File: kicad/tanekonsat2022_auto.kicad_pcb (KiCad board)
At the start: 2 copper layers, 88 parts, among them IC1 W25Q128JVSIQ, IC2 ADP3338AKCZ-3.3-RL, IC3 NJM12888F18, IC4 TESEO-LIV3F, IC5 CGGBPD.25.A, IC6 MAX2641EUT+T, IC7 TB67H450FNG,EL, IC8 TB67H450FNG,EL, J1 Conn_01x02_Male, J2 USB_B_Micro, J3 Conn_01x02_Male, J4 Conn_01x02_Male, J5 Conn_01x06_Female, J6 Conn_01x06_Female, J7 Conn_01x04_Female, Q1 Q_NMOS_DGS, Q2 Q_NMOS_DGS, Q3 BSS138, Q4 BSS138, Q5 BSS138, Q6 BSS138, Q7 Q_NMOS_DGS, SW1 SW_DIP_x01, U1 RP2040, U2 CR1025, U3 VL53L5X_SL, U4 ICM-20948_SL, Y1 FA-238V_12.0000MB-K3

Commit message: done! AW of GNSS board
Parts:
- removed C26: 56p, Capacitor_SMD:C_0201_0603Metric
- added J8: Conn_01x02_Female, Connector_PinHeader_2.00mm:PinHeader_1x02_P2.00mm_Vertical, F.Cu at (177.6, 49.7)
- C19, C20, C21, D1, D2, IC2, IC7, IC8, R18, R19, R20, R21: moved to B.Cu
- C2, C5: value 27p -> 10p
- J1: footprint Connector_JST:JST_PH_B3B-PH-K_1x03_P2.00mm_Vertical -> Connector_JST:JST_PH_S3B-PH-K_1x03_P2.00mm_Horizontal; moved to B.Cu
- J3, J4: footprint Connector_PinHeader_2.00mm:PinHeader_1x02_P2.00mm_Vertical -> tanekonsat:PinHeader_1x02_P2.00mm_Vertical
- J5, J6: footprint Connector_PinHeader_2.00mm:PinHeader_1x06_P2.00mm_Vertical -> tanekonsat:PinHeader_1x06_P2.00mm_Vertical; moved to B.Cu
- moved J5 93.3 mm to (129.2, 91.4), turned to -90 degrees
- moved U3 89.5 mm to (138.4, 60.0)
- moved J6 82.2 mm to (116.2, 91.4), turned to -90 degrees
- moved C21 79.0 mm to (116.1, 86.4)
- moved C20 75.5 mm to (107.9, 75.2), turned to 180 degrees
- moved C29 71.8 mm to (169.0, 51.1)
- moved Q2 69.8 mm to (80.5, 86.9)
- moved L2 69.8 mm to (173.7, 54.5)
- moved C27 69.1 mm to (171.1, 49.1), turned to 90 degrees
- moved R19 67.6 mm to (125.6, 89.2), turned to 180 degrees
- moved C18 66.3 mm to (115.6, 88.9), turned to 90 degrees
- moved IC1 66.0 mm to (134.4, 74.7), turned to -90 degrees
- moved C19 64.3 mm to (107.9, 77.7), turned to 180 degrees
- moved R20 63.5 mm to (126.5, 85.9)
- moved IC7 62.9 mm to (131.1, 86.1), turned to -90 degrees
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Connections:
- C29 pad 1: +3V3 -> /VCC_RF
- C29 pad 2: +3V3 -> GND2
- IC4 pad 14: Net-(C26-Pad1) -> /VCC_RF
- IC4 pad 16: unconnected-(IC4-Pad16) -> Net-(IC4-Pad16)
- IC4 pad 17: unconnected-(IC4-Pad17) -> Net-(IC4-Pad17)
- IC6 pad 6: +3V3 -> /VCC_RF
- IC7 pad 3: /GPIO13_MO_A_2 -> /GPIO12_MO_A_1
- IC7 pad 6: Net-(IC7-Pad6) -> /M1_MINUS
- IC7 pad 8: Net-(IC7-Pad8) -> /M1_PLUS
- IC8 pad 2: /GPIO14_MO_B_1 -> /GPIO15_MO_B_2
- IC8 pad 3: /GPIO15_MO_B_2 -> /GPIO14_MO_B_1
- IC8 pad 6: Net-(IC8-Pad6) -> /M2_MINUS
- IC8 pad 8: Net-(IC8-Pad8) -> /M2_PLUS
- J5 pad 1: /GPIO13_MO_A_2 -> /M1_PLUS
- J5 pad 2: /GPIO13_MO_A_2 -> /M1_MINUS
- J5 pad 4: /GPIO21_MOE_A_1 -> /GPIO20_MOE_A_1
- J5 pad 5: /GPIO20_MOE_A_2 -> /GPIO21_MOE_A_2
- J6 pad 1: /GPIO14_MO_B_1 -> /M2_PLUS
- J6 pad 2: /GPIO15_MO_B_2 -> /M2_MINUS
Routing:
- net +3V0: track 0.00 -> 30.9 mm
- net GND2: track 0.00 -> 23.4 mm, vias 0 -> 101
- net /VCC_RF: track 0.00 -> 13.5 mm
- net +3V3: track 0.00 -> 5.58 mm
- net Net-(C28-Pad2): track 0.00 -> 3.73 mm
- net /GPIO4_GNSS_TX: track 0.00 -> 3.36 mm
- net Net-(C24-Pad1): track 0.00 -> 3.35 mm
- net Net-(IC4-Pad16): track 0.00 -> 3.05 mm
- net /GPIO5_GNSS_RX: track 0.00 -> 2.99 mm
- net Net-(IC4-Pad17): track 0.00 -> 2.67 mm
- net Net-(C28-Pad1): track 0.00 -> 1.96 mm
- net Net-(IC6-Pad1): track 0.00 -> 1.68 mm
- net Net-(C27-Pad2): track 0.00 -> 1.60 mm
- net Net-(C27-Pad1): track 0.00 -> 1.40 mm
- net Net-(C25-Pad2): track 0.00 -> 1.27 mm
- added copper zone on B.Cu, net GND2
- added copper zone on F.Cu, net GND2
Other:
- board outline added: 76.6 x 67.8 mm
- board text added: "+3V3"
- board text added: "DERC"
- board text added: "Design: Akio M"
- board text added: "GND"
- board text added: "GNSS Board"
- board text added: "I2C"
- board text added: "RX"
- board text added: "SCL"
- board text added: "SDA"
- board text added: "TX"
- board text added: "UART"
- board text added: "tanekonsat2022"

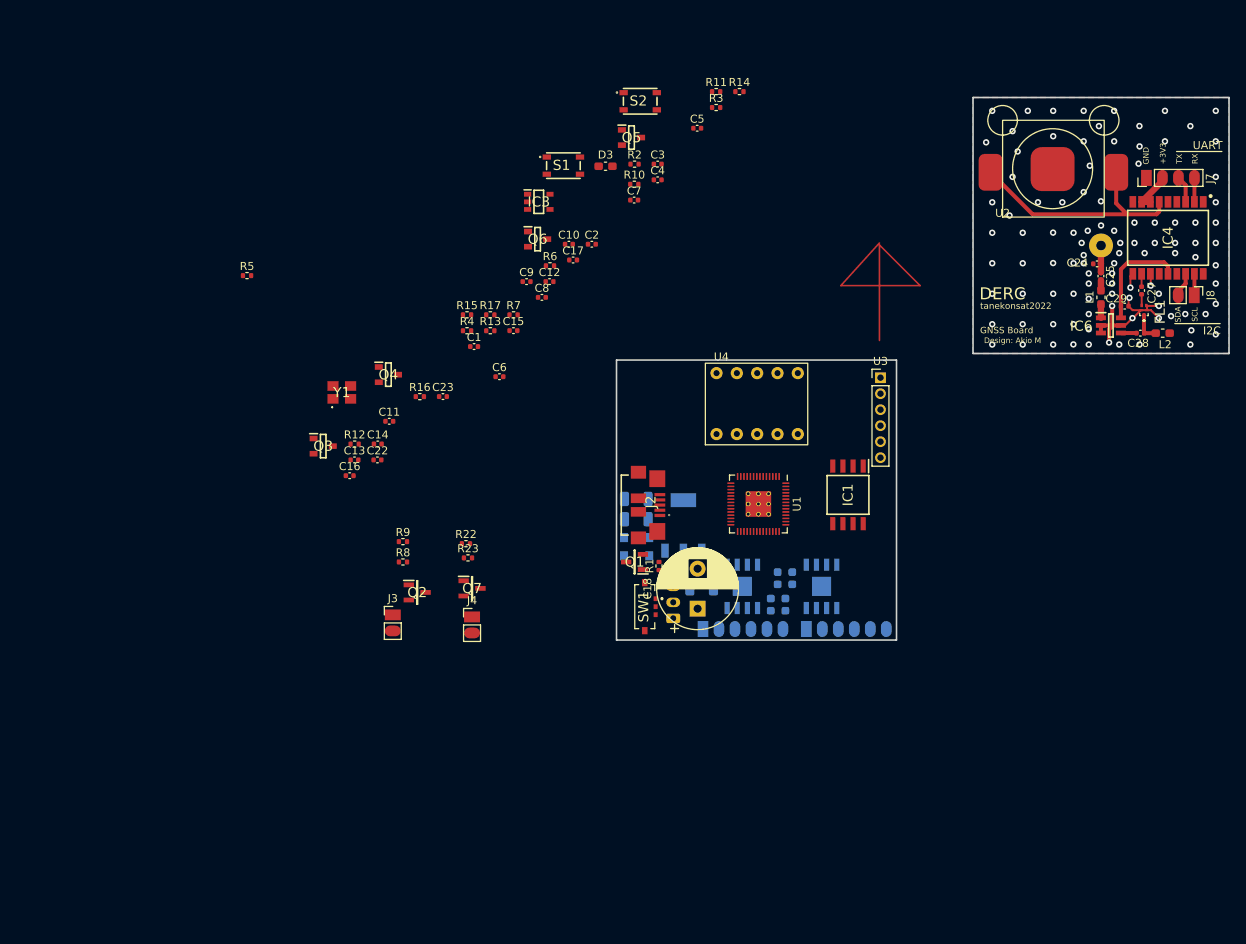
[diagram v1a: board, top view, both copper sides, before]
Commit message: update 9-axis sensor
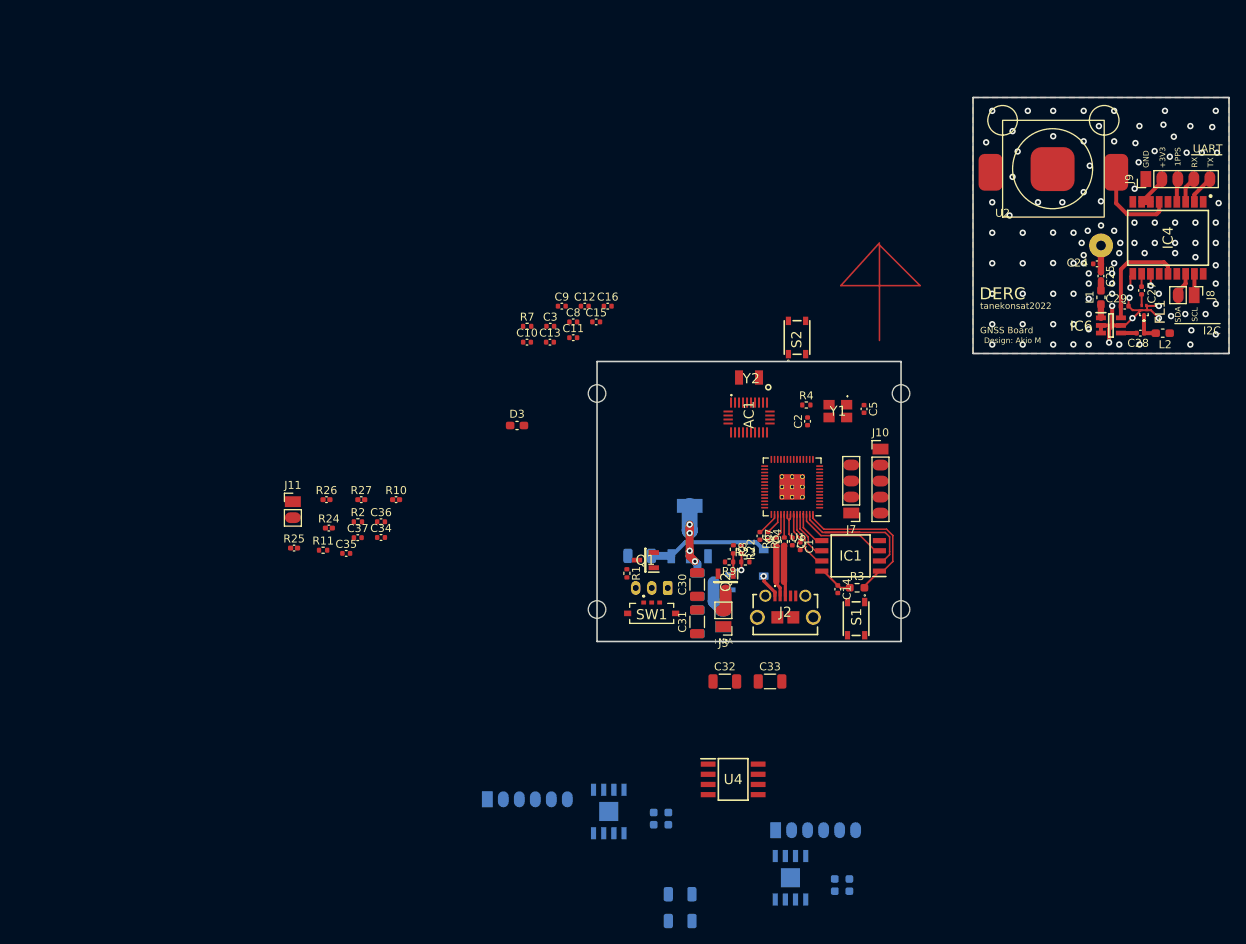
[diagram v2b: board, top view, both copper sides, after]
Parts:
- removed C17, C23: 1u, Capacitor_SMD:C_0402_1005Metric
- removed C22: 0.01u, Capacitor_SMD:C_0402_1005Metric
- removed D2: SS2040FL_R1_00001, SamacSys_Parts:SODFL3618X110N
- removed IC3: NJM12888F18, SamacSys_Parts:SOT95P280X130-5N
- removed Q3, Q4, Q5, Q6: BSS138, SamacSys_Parts:SOT95P240X120-3N
- removed R12, R13, R14, R15, R16, R17: 10k, Resistor_SMD:R_0402_1005Metric
- removed U3: VL53L5X_SL, Connector_PinHeader_2.00mm:PinHeader_1x06_P2.00mm_Vertical
- added AC1: BNO085, tanekonsat:BNO085, F.Cu at (122.0, 65.0)
- added C26: 100u, Capacitor_SMD:C_1206_3216Metric, B.Cu at (113.4, 127.9)
- added C30: 100u, Capacitor_SMD:C_1206_3216Metric, F.Cu at (115.5, 85.9)
- added C31: 100u, Capacitor_SMD:C_1206_3216Metric, F.Cu at (115.5, 90.6)
- added C32: 100u, Capacitor_SMD:C_1206_3216Metric, F.Cu at (119.0, 98.0)
- added C33: 100u, Capacitor_SMD:C_1206_3216Metric, F.Cu at (124.6, 98.0)
- added C34: 100n, Capacitor_SMD:C_0402_1005Metric, F.Cu at (76.0, 80.0)
- added C35: 22p, Capacitor_SMD:C_0402_1005Metric, F.Cu at (71.7, 82.0)
- added C36: 22p, Capacitor_SMD:C_0402_1005Metric, F.Cu at (76.0, 78.0)
- added C37: 100n, Capacitor_SMD:C_0402_1005Metric, F.Cu at (73.1, 80.0)
- added J10: Conn_01x05_Female, tanekonsat:PinHeader_1x05_P2.00mm_Vertical, F.Cu at (138.4, 68.9)
- added J11: Conn_01x02_Female, tanekonsat:PinHeader_1x02_P2.00mm_Vertical, F.Cu at (65.0, 75.5)
- added J9: Conn_01x05_Female, tanekonsat:PinHeader_1x05_P2.00mm_Vertical, F.Cu at (171.6, 35.2)
- added R24: 0, tanekonsat:Jumper_0402_1005Metric, F.Cu at (69.5, 78.8)
- added R25: 0, tanekonsat:Jumper_0402_1005Metric, F.Cu at (65.1, 81.3)
- added R26: 0, tanekonsat:Jumper_0402_1005Metric, F.Cu at (69.2, 75.3)
- added R27: 0, tanekonsat:Jumper_0402_1005Metric, F.Cu at (73.5, 75.3)
- added REF**: MountingHole_2.2mm_M2, MountingHole:MountingHole_2.2mm_M2, F.Cu at (141.0, 89.0)
- added REF**: MountingHole_2.2mm_M2, MountingHole:MountingHole_2.2mm_M2, F.Cu at (103.0, 89.0)
- added REF**: MountingHole_2.2mm_M2, MountingHole:MountingHole_2.2mm_M2, F.Cu at (141.0, 62.0)
- added REF**: MountingHole_2.2mm_M2, MountingHole:MountingHole_2.2mm_M2, F.Cu at (103.0, 62.0)
- added Y2: FC-135_32.768KHz_7pF_+_-20ppm, SamacSys_Parts:FC-135, F.Cu at (122.0, 60.0)
- C18: value 1000u -> 100u; footprint Capacitor_THT:CP_Radial_D10.0mm_P5.00mm -> Capacitor_SMD:C_1206_3216Metric; moved to B.Cu
- D1: value SS2040FL_R1_00001 -> 1N4148W; footprint SamacSys_Parts:SODFL3618X110N -> Diode_SMD:D_SOD-123
- J2: footprint SamacSys_Parts:ZX62R-B-5P_30_ -> SamacSys_Parts:101181940001LFBKN
- J4, Q7: moved to B.Cu
- J7: footprint Connector_PinHeader_2.00mm:PinHeader_1x04_P2.00mm_Vertical -> tanekonsat:PinHeader_1x04_P2.00mm_Vertical
- R10: value 10k -> 0; footprint Resistor_SMD:R_0402_1005Metric -> tanekonsat:Jumper_0402_1005Metric
- R3: value 10k -> DNF; footprint Resistor_SMD:R_0402_1005Metric -> Resistor_SMD:R_0603_1608Metric_Pad0.98x0.95mm_HandSolder
- U4: value ICM-20948_SL -> ACPL-224-500E; footprint tanekonsat:ICM-20948_SL -> SamacSys_Parts:SOIC127P700X220-8N
- moved R11 75.5 mm to (68.8, 81.6)
- moved R5 74.9 mm to (126.4, 80.5), turned to 90 degrees
- moved S1 67.4 mm to (135.4, 90.1), turned to -90 degrees
- moved R3 62.6 mm to (135.5, 86.3)
- moved Y1 62.0 mm to (133.1, 64.2), turned to 180 degrees
- moved C14 60.3 mm to (133.1, 86.5), turned to -90 degrees
- moved R2 56.5 mm to (73.1, 78.0)
- moved J7 55.8 mm to (134.8, 76.9), turned to 180 degrees
- moved R10 49.4 mm to (77.9, 75.3)
- moved C1 47.8 mm to (128.4, 81.1), turned to -90 degrees
- moved C4 46.6 mm to (124.4, 79.8), turned to -90 degrees
- moved C7 44.8 mm to (123.4, 79.8), turned to -90 degrees
- moved R6 44.6 mm to (125.4, 80.5), turned to 90 degrees
- moved R4 43.4 mm to (129.2, 63.4)
- moved C6 42.0 mm to (127.4, 80.5), turned to -90 degrees
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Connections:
- net /GPIO24_Nichrome renamed /GPIO24_NichromeB
- net /GPIO4_GNSS_TX renamed /GPIO4_GNSS_RX
- net /GPIO5_GNSS_RX renamed /GPIO5_GNSS_TX
- C18 pad 1: /+7V4 -> /V_REG
- C2 pad 1: Net-(C2-Pad1) -> GND
- C2 pad 2: GND -> /XIN
- C21 pad 1: +3V3 -> /V_REG
- D1 pad 2: /+7V4 -> /VBUS
- IC4 pad 4: unconnected-(IC4-Pad4) -> /GNSS_1PPS
- IC7 pad 2: /GPIO13_MO_A_2 -> Net-(IC7-Pad2)
- IC7 pad 3: /GPIO12_MO_A_1 -> Net-(IC7-Pad3)
- IC7 pad 5: /+7V4 -> /V_REG
- IC8 pad 2: /GPIO15_MO_B_2 -> Net-(IC8-Pad2)
- IC8 pad 3: /GPIO14_MO_B_1 -> Net-(IC8-Pad3)
- IC8 pad 5: /+7V4 -> /V_REG
- J1 pad 1: /+7V4 -> /V_REG
- J3 pad 1: /+7V4 -> /V_REG
- J4 pad 1: /+7V4 -> /V_REG
- R10 pad 1: +3V3 -> GND
- R10 pad 2: /GPIO18_M_SCK -> GND3
- R11 pad 2: /GPIO19_M_SDI_RX -> Net-(AC1-Pad4)
- R4 pad 2: Net-(R4-Pad2) -> Net-(C5-Pad1)
- R7 pad 1: /GPIO25_LED -> /GPIO3_LED
- R8 pad 1: /GPIO3_Nichrome -> /GPIO25_NichromeA
- SW1 pad 2: /+7V4 -> /V_REG
- U1 pad 13: /GPIO10 -> /GPIO10_I2C_EXT_SDA
- U1 pad 14: /GPIO11 -> /GPIO11_I2C_EXT_SCL
- U1 pad 27: /GPIO16_M_SDO_TX -> /GPIO16_IMU_MISO
- U1 pad 28: /GPIO17_M_CS -> /GPIO17_IMU_CS
- U1 pad 29: /GPIO18_M_SCK -> /GPIO18_IMU_SCK
- U1 pad 30: /GPIO19_M_SDI_RX -> /GPIO19_IMU_MOSI
- U1 pad 37: /GPIO25_LED -> /GPIO25_NichromeA
- U1 pad 5: /GPIO3_Nichrome -> /GPIO3_LED
- U1 pad 8: /GPIO6 -> /GPIO6_IMU_INT
- U1 pad 9: /GPIO7 -> /GPIO7_IMU_RST
- U4 pad 1: +1V8 -> /GPIO13_MO_A_2
- U4 pad 2: +1V8 -> /GPIO12_MO_A_1
- U4 pad 3: /IMU_SCLK -> /GPIO15_MO_B_2
- U4 pad 4: /IMU_SDI -> /GPIO14_MO_B_1
- U4 pad 5: /IMU_SDO -> Net-(IC8-Pad3)
- U4 pad 6: /IMU_CS -> Net-(IC8-Pad2)
- U4 pad 7: unconnected-(U4-Pad7) -> Net-(IC7-Pad3)
- U4 pad 8: unconnected-(U4-Pad8) -> Net-(IC7-Pad2)
- Y1 pad 1: Net-(R4-Pad2) -> Net-(C5-Pad1)
- Y1 pad 2: Net-(C2-Pad1) -> GND
- Y1 pad 4: Net-(C5-Pad1) -> GND
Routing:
- net +3V3: track 5.58 -> 28.9 mm, vias 0 -> 4
- net /QSPI_SD1: track 0.00 -> 19.8 mm
- net /QSPI_SS: track 0.00 -> 19.6 mm
- net +3V0: track 30.9 -> 11.7 mm
- net /V_REG: track 0.00 -> 15.2 mm
- net /QSPI_SD2: track 0.00 -> 11.5 mm
- net /QSPI_SD3: track 0.00 -> 7.42 mm
- net +1V1: track 0.00 -> 6.98 mm
- net /USB_D-: track 0.00 -> 6.24 mm
- net /QSPI_SCLK: track 0.00 -> 6.14 mm
- net /USB_D+: track 0.00 -> 6.13 mm
- net /QSPI_SD0: track 0.00 -> 4.83 mm
- net Net-(J4-Pad2): track 0.00 -> 4.06 mm
- net Net-(Q7-Pad1): track 0.00 -> 3.68 mm, vias 0 -> 1
- net Net-(R6-Pad2): track 0.00 -> 3.15 mm
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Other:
- board size 76.6 x 67.8 mm -> 79 x 68 mm
- board text added: "1PPS"

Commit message: done AW of main board
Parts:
- removed C31, C32: 100u, Capacitor_SMD:C_1206_3216Metric
- removed R24, R25, R26, R27: 0, tanekonsat:Jumper_0402_1005Metric
- removed U4: ACPL-224-500E, SamacSys_Parts:SOIC127P700X220-8N
- added ?: , , F.Cu at (111.1, 83.6)
- added ?: , , F.Cu at (141.0, 89.0)
- added C17: 100u, Capacitor_SMD:C_1206_3216Metric, B.Cu at (121.9, 86.5)
- added C22: 100u, Capacitor_SMD:C_1206_3216Metric, B.Cu at (111.1, 62.4)
- added C23: 100u, Capacitor_SMD:C_1206_3216Metric, B.Cu at (137.6, 76.4)
- added M1: Motor_DC, tanekonsat:PinHeader_1x02_P2.00mm_Vertical, B.Cu at (133.4, 59.6)
- added M2: Motor_DC, tanekonsat:PinHeader_1x02_P2.00mm_Vertical, B.Cu at (106.3, 59.4)
- added R12: 100, Capacitor_SMD:C_0603_1608Metric, B.Cu at (115.3, 73.2)
- added R13: 1k, Capacitor_SMD:C_0603_1608Metric, F.Cu at (113.2, 67.8)
- added R14: 3k, Capacitor_SMD:C_0603_1608Metric, F.Cu at (110.3, 79.5)
- added R15: 1k, Capacitor_SMD:C_0603_1608Metric, F.Cu at (110.3, 76.5)
- added REF**: PinHeader_1x01_P2.54mm_Vertical, Connector_PinHeader_2.54mm:PinHeader_1x01_P2.54mm_Vertical, B.Cu at (137.5, 59.5)
- added REF**: PinHeader_1x01_P2.54mm_Vertical, Connector_PinHeader_2.54mm:PinHeader_1x01_P2.54mm_Vertical, B.Cu at (111.2, 59.6)
- added U5: LT6106, Package_TO_SOT_SMD:SOT-23-5, F.Cu at (119.9, 74.3)
- added U6: Opamp_Dual, Package_SO:SSOP-8_5.25x5.24mm_P1.27mm, F.Cu at (114.6, 73.4)
- AC1: footprint tanekonsat:BNO085 -> SamacSys_Parts:BNO085
- C1, C10, C12, C14, C16, C24, C25, C27, C28, C29, C34, C35, C36, C37, C4, C7: footprint Capacitor_SMD:C_0402_1005Metric -> Capacitor_SMD:C_0603_1608Metric
- C11, C13, C15, C2, C3, C6, C8, C9: footprint Capacitor_SMD:C_0402_1005Metric -> Capacitor_SMD:C_0603_1608Metric; moved to B.Cu
- C21, C26, IC7, IC8: moved to F.Cu
- C33, J11: moved to B.Cu
- C5: value 10p -> 100u; footprint Capacitor_SMD:C_0402_1005Metric -> Capacitor_SMD:C_1206_3216Metric; moved to B.Cu
- D3: footprint Capacitor_SMD:C_0603_1608Metric_Pad1.08x0.95mm_HandSolder -> Capacitor_SMD:C_0603_1608Metric
- J5, J6: value Conn_01x06_Female -> Conn_01x04_Male; footprint tanekonsat:PinHeader_1x06_P2.00mm_Vertical -> tanekonsat:PinHeader_1x04_P2.00mm_Vertical
- R1, R11, R2, R22, R23, R5, R6, R8, R9: footprint Resistor_SMD:R_0402_1005Metric -> Capacitor_SMD:C_0603_1608Metric
- R10: value 0 -> 0.01; footprint tanekonsat:Jumper_0402_1005Metric -> Resistor_SMD:R_1206_3216Metric
- R4: value 1k -> 10k; footprint Resistor_SMD:R_0402_1005Metric -> Capacitor_SMD:C_0603_1608Metric
- R7: value 660 -> 1k; footprint Resistor_SMD:R_0402_1005Metric -> Capacitor_SMD:C_0603_1608Metric; moved to B.Cu
- Y1: value FA-238V_12.0000MB-K3 -> SIT2001BI-S2-33E-12.000000D; footprint SamacSys_Parts:FA238V120000MBK3 -> Package_TO_SOT_SMD:SOT-23-5
- moved J11 74.5 mm to (139.2, 69.1), turned to 180 degrees
- moved R2 63.3 mm to (135.6, 87.8), turned to 180 degrees
- moved R20 61.3 mm to (132.6, 62.9), turned to 90 degrees
- moved IC7 61.0 mm to (135.0, 62.0), turned to 90 degrees
- moved R18 59.7 mm to (134.1, 62.9), turned to 90 degrees
- moved C35 58.2 mm to (125.2, 59.1)
- moved R19 53.5 mm to (107.8, 62.5), turned to 90 degrees
- moved IC8 52.1 mm to (108.1, 62.3), turned to 90 degrees
- moved R21 52.1 mm to (106.3, 62.5), turned to 90 degrees
- moved R11 51.6 mm to (117.5, 64.5), turned to -90 degrees
- moved C8 51.0 mm to (138.0, 87.1), turned to -90 degrees
- moved C37 48.1 mm to (117.5, 61.5), turned to 90 degrees
- moved C34 46.1 mm to (120.4, 67.8)
- moved C36 46.0 mm to (117.9, 59.2), turned to 180 degrees
- moved R7 44.6 mm to (133.1, 75.5)
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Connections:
- AC1 pad 10: Net-(AC1-Pad10) -> GND
- AC1 pad 11: /GPIO7_IMU_RST -> /GPIO17_IMU_RST
- AC1 pad 14: /GPIO6_IMU_INT -> /GPIO16_IMU_INT
- AC1 pad 17: /GPIO19_IMU_MOSI -> /GPIO15_IMU_MOSI
- AC1 pad 18: /GPIO17_IMU_CS -> /GPIO13_IMU_CS
- AC1 pad 19: /GPIO18_IMU_SCK -> /GPIO14_IMU_SCK
- AC1 pad 2: Net-(AC1-Pad2) -> GND
- AC1 pad 20: /GPIO16_IMU_MISO -> /GPIO12_IMU_MISO
- AC1 pad 25: Net-(AC1-Pad25) -> GND
- AC1 pad 28: Net-(AC1-Pad28) -> +3V3
- AC1 pad 3: Net-(AC1-Pad28) -> +3V3
- C16 pad 1: +3V3 -> /3V3_REG_OUT
- C18 pad 1: /V_REG -> /+7V4
- C19 pad 1: /V_REG -> /+7V4
- C2 pad 1: GND -> /XIN
- C2 pad 2: /XIN -> GND
- C21 pad 1: /V_REG -> /+7V4
- C24 pad 2: GND2 -> GND
- C26 pad 1: /V_REG -> /+7V4
- C29 pad 2: GND2 -> GND
- C30 pad 1: /V_REG -> /+7V4
- C33 pad 1: /V_REG -> +3V3
- C37 pad 1: Net-(AC1-Pad28) -> +3V3
- C5 pad 1: Net-(C5-Pad1) -> /+7V4
- C9 pad 1: +3V3 -> /3V3_REG_OUT
- D1 pad 1: /V_REG -> /+7V4
- FL1 pad 2: GND2 -> GND
- FL1 pad 3: GND2 -> GND
- FL1 pad 5: GND2 -> GND
- IC2 pad 2: +3V3 -> /3V3_REG_OUT
- IC2 pad 3: /V_REG -> /+7V4
- IC2 pad 4: +3V3 -> /3V3_REG_OUT
- IC4 pad 1: GND2 -> GND
- IC4 pad 10: GND2 -> GND
- IC4 pad 12: GND2 -> GND
- IC6 pad 2: GND2 -> GND
- IC6 pad 3: GND2 -> GND
- IC6 pad 5: GND2 -> GND
- IC7 pad 1: GND3 -> GND
- IC7 pad 2: Net-(IC7-Pad2) -> /GPIO11_MO_A_2
- IC7 pad 3: Net-(IC7-Pad3) -> /GPIO10_MO_A_1
- IC7 pad 5: /V_REG -> /+7V4
- IC8 pad 1: GND3 -> GND
- IC8 pad 2: Net-(IC8-Pad2) -> /GPIO19_MO_B_2
- IC8 pad 3: Net-(IC8-Pad3) -> /GPIO18_MO_B_1
- IC8 pad 5: /V_REG -> /+7V4
- J1 pad 1: /V_REG -> /+7V4
- J10 pad 1: /GPIO9_ToF_SCL -> /GPIO7_ToF_SCL
- J10 pad 2: /GPIO2_ToF_RST -> /GPIO3_ToF_RST
- J10 pad 3: /GPIO8_ToF_SDA -> /GPIO6_ToF_SDA
- J11 pad 1: /GPIO11_I2C_EXT_SCL -> /GPIO9_I2C_EXT_SCL
- J11 pad 2: /GPIO10_I2C_EXT_SDA -> /GPIO8_I2C_EXT_SDA
- J3 pad 1: /V_REG -> /+7V4
- J4 pad 1: /V_REG -> /+7V4
- J5 pad 1: /M1_PLUS -> GND
- J5 pad 2: /M1_MINUS -> /GPIO23_MOE_B_2
- J5 pad 3: +3V3 -> /GPIO21_MOE_B_1
- J5 pad 4: /GPIO20_MOE_A_1 -> +3V3
- J6 pad 1: /M2_PLUS -> GND
- J6 pad 2: /M2_MINUS -> /GPIO22_MOE_A_2
- J6 pad 3: +3V3 -> /GPIO20_MOE_A_1
- J6 pad 4: /GPIO22_MOE_B_1 -> +3V3
- J7 pad 1: GND2 -> GND
- J9 pad 1: GND2 -> GND
- L2 pad 2: GND2 -> GND
- R1 pad 1: Net-(Q1-Pad1) -> Net-(R1-Pad1)
- R10 pad 1: GND -> /3V3_REG_OUT
- R10 pad 2: GND3 -> +3V3
- R18 pad 1: GND3 -> GND
- R19 pad 1: GND3 -> GND
- R20 pad 1: GND3 -> GND
- R21 pad 1: GND3 -> GND
- R22 pad 1: /GPIO24_NichromeB -> /GPIO29_NichromeB
- R4 pad 1: /XOUT -> Net-(R1-Pad1)
- R4 pad 2: Net-(C5-Pad1) -> Net-(Q1-Pad1)
- R7 pad 1: /GPIO3_LED -> /GPIO2_LED
- R8 pad 1: /GPIO25_NichromeA -> /GPIO28_NichromeA
- SW1 pad 2: /V_REG -> /+7V4
- SW1 pad C1: Net-(Q1-Pad1) -> Net-(R1-Pad1)
- U1 pad 11: /GPIO8_ToF_SDA -> /GPIO8_I2C_EXT_SDA
- U1 pad 12: /GPIO9_ToF_SCL -> /GPIO9_I2C_EXT_SCL
- U1 pad 13: /GPIO10_I2C_EXT_SDA -> /GPIO10_MO_A_1
- U1 pad 14: /GPIO11_I2C_EXT_SCL -> /GPIO11_MO_A_2
- U1 pad 15: /GPIO12_MO_A_1 -> /GPIO12_IMU_MISO
- U1 pad 16: /GPIO13_MO_A_2 -> /GPIO13_IMU_CS
- U1 pad 17: /GPIO14_MO_B_1 -> /GPIO14_IMU_SCK
- U1 pad 18: /GPIO15_MO_B_2 -> /GPIO15_IMU_MOSI
- U1 pad 27: /GPIO16_IMU_MISO -> /GPIO16_IMU_INT
- U1 pad 28: /GPIO17_IMU_CS -> /GPIO17_IMU_RST
- U1 pad 29: /GPIO18_IMU_SCK -> /GPIO18_MO_B_1
- U1 pad 30: /GPIO19_IMU_MOSI -> /GPIO19_MO_B_2
- U1 pad 32: /GPIO21_MOE_A_2 -> /GPIO21_MOE_B_1
- U1 pad 34: /GPIO22_MOE_B_1 -> /GPIO22_MOE_A_2
- U1 pad 36: /GPIO24_NichromeB -> unconnected-(U1-Pad36)
- U1 pad 37: /GPIO25_NichromeA -> unconnected-(U1-Pad37)
- U1 pad 38: /GPIO26_ADC0 -> /GPIO26_ADC_I_monitor
- U1 pad 39: /GPIO27_ADC1 -> /GPIO27_ADC_V_monitor
- U1 pad 4: /GPIO2_ToF_RST -> /GPIO2_LED
- U1 pad 40: /GPIO28_ADC2 -> /GPIO28_NichromeA
- U1 pad 41: /GPIO29_ADC3 -> /GPIO29_NichromeB
- U1 pad 5: /GPIO3_LED -> /GPIO3_ToF_RST
- U1 pad 8: /GPIO6_IMU_INT -> /GPIO6_ToF_SDA
- U1 pad 9: /GPIO7_IMU_RST -> /GPIO7_ToF_SCL
- U2 pad 1: GND2 -> GND
- Y1 pad 1: Net-(C5-Pad1) -> GND
- Y1 pad 2: GND -> unconnected-(Y1-Pad2)
- Y1 pad 3: /XIN -> unconnected-(Y1-Pad3)
- Y1 pad 4: GND -> +3V3
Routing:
- net GND: track 0.00 -> 296.3 mm, vias 0 -> 280
- net +3V3: track 28.9 -> 152.2 mm, vias 4 -> 12
- net /+7V4: track 0.00 -> 66.0 mm, vias 0 -> 9
- net GND2: track 22.6 -> 0.00 mm, vias 107 -> 0
- net /RUN: track 0.00 -> 22.4 mm, vias 0 -> 4
- net /GPIO21_MOE_B_1: track 0.00 -> 22.1 mm, vias 0 -> 1
- net /GPIO23_MOE_B_2: track 0.00 -> 21.6 mm, vias 0 -> 1
- net /3V3_REG_OUT: track 0.00 -> 19.9 mm, vias 0 -> 6
- net /GPIO19_MO_B_2: track 0.00 -> 19.7 mm, vias 0 -> 2
- net /GPIO20_MOE_A_1: track 0.00 -> 18.4 mm, vias 0 -> 1
- net /GPIO18_MO_B_1: track 0.00 -> 18.3 mm, vias 0 -> 2
- net /GPIO22_MOE_A_2: track 0.00 -> 17.7 mm, vias 0 -> 1
- net /GPIO26_ADC_I_monitor: track 0.00 -> 15.2 mm, vias 0 -> 2
- net /V_REG: track 15.2 -> 0.00 mm
- net Net-(R13-Pad1): track 0.00 -> 13.8 mm, vias 0 -> 2
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- added copper zone on F.Cu, net +1V1
- added copper zone on F.Cu, net +3V3
- added copper zone on B.Cu, net GND
- added copper zone on F.Cu, net GND
- removed copper zone on B.Cu, net GND2
- removed copper zone on F.Cu, net GND2
